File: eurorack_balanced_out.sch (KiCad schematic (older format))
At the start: 19 parts

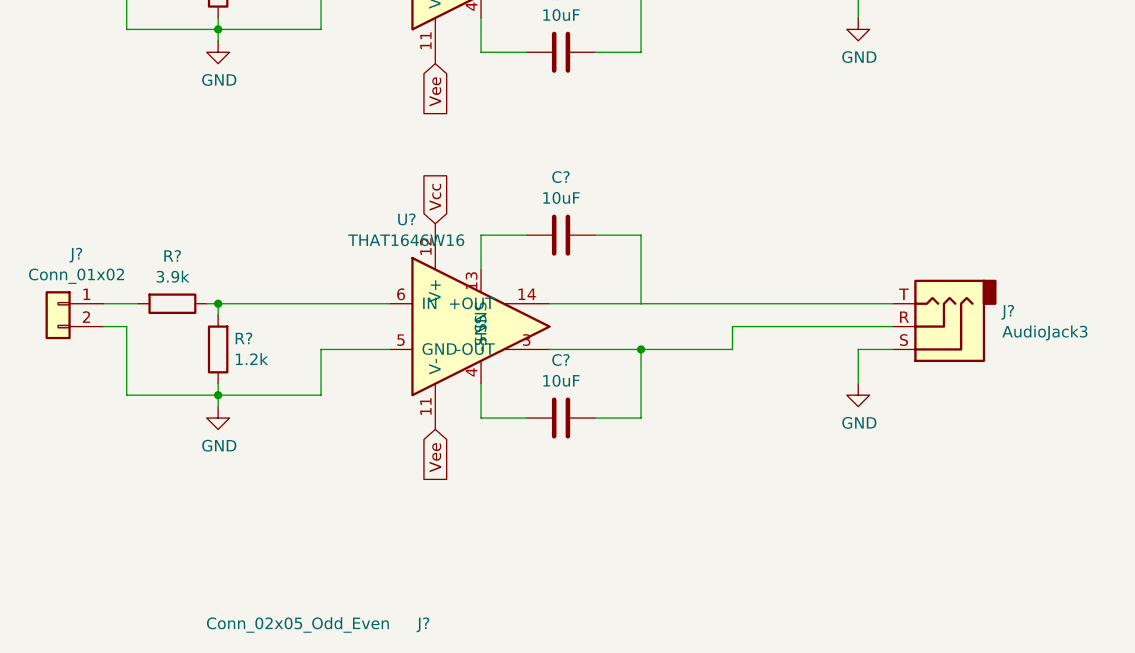
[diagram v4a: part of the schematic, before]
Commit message: delete a channel
we'll duplicate it again when we're done
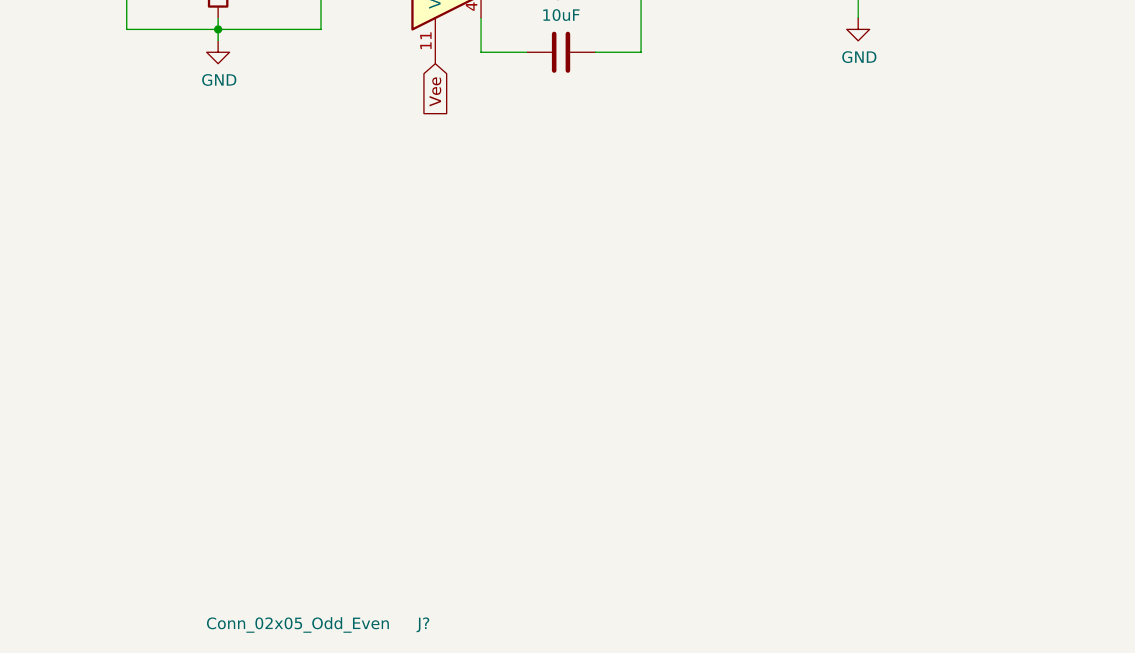
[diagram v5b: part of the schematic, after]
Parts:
- removed C? (x2): 10uF, Capacitor_SMD:CP_Elec_5x5.4, symbol Device:C
- removed J?: Conn_01x02, symbol Connector_Generic:Conn_01x02
- removed J?: AudioJack3, Connector_Audio:Jack_6.35mm_Neutrik_NJ3FD-V_Vertical, symbol Connector:AudioJack3
- removed R?: 1.2k, Resistor_SMD:R_0805_2012Metric_Pad1.15x1.40mm_HandSolder, symbol Device:R
- removed R?: 3.9k, Resistor_SMD:R_0805_2012Metric_Pad1.15x1.40mm_HandSolder, symbol Device:R
- removed U?: THAT1646W16, Package_SO:SOIC-16W_7.5x10.3mm_P1.27mm, symbol patchut:THAT1646W16
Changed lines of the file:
@@
 $EndComp
-$Comp
-L patchut:THAT1646W16 U?
-U 1 1 5EC6EB1D
-P 5000 3000
-F 0 "U?" H 4675 3467 50  0000 C CNN
-F 1 "THAT1646W16" H 4675 3376 50  0000 C CNN
-F 2 "Package_SO:SOIC-16W_7.5x10.3mm_P1.27mm" H 4850 3350 50  0001 C CNN
-F 3 "http://www.thatcorp.com/datashts/THAT_1606-1646_Datasheet.pdf" H 4850 3350 50  0001 C CNN
-	1    5000 3000
-	1    0    0    -1
-$EndComp
-$Comp
-L Device:C C?
-U 1 1 5EC6EB24
-P 5350 2600
-F 0 "C?" V 5098 2600 50  0000 C CNN
-F 1 "10uF" V 5189 2600 50  0000 C CNN
-F 2 "Capacitor_SMD:CP_Elec_5x5.4" H 5388 2450 50  0001 C CNN
-F 3 "~" H 5350 2600 50  0001 C CNN
-F 4 "647-UWP1C100MCL" V 5350 2600 50  0001 C CNN "Mouser"
-	1    5350 2600
-	0    1    1    0
-$EndComp
-Wire Wire Line
-	5200 2600 5000 2600
-Wire Wire Line
-	5000 2600 5000 2750
-Wire Wire Line
-	5300 2900 5700 2900
-Wire Wire Line
-	5700 2900 5700 2600
-Wire Wire Line
-	5700 2600 5500 2600
-$Comp
-L Device:C C?
-U 1 1 5EC6EB30
-P 5350 3400
-F 0 "C?" V 5098 3400 50  0000 C CNN
-F 1 "10uF" V 5189 3400 50  0000 C CNN
-F 2 "Capacitor_SMD:CP_Elec_5x5.4" H 5388 3250 50  0001 C CNN
-F 3 "~" H 5350 3400 50  0001 C CNN
-F 4 "647-UWP1C100MCL" V 5350 3400 50  0001 C CNN "Mouser"
-	1    5350 3400
-	0    1    1    0
-$EndComp
-Wire Wire Line
-	5000 3250 5000 3400
-Wire Wire Line
-	5000 3400 5200 3400
-Wire Wire Line
-	5500 3400 5700 3400
-Wire Wire Line
-	5700 3400 5700 3100
-Wire Wire Line
-	5700 3100 5300 3100
-Text GLabel 4800 3450 3    50   Input ~ 0
-Vee
-Text GLabel 4800 2550 1    50   Input ~ 0
-Vcc
 $Comp
 L Connector_Generic:Conn_02x05_Odd_Even J?
@@
 	3850 1700 4300 1700
 $Comp
-L power:GND #PWR?
-U 1 1 5ECB48AD
-P 3850 3350
-F 0 "#PWR?" H 3850 3100 50  0001 C CNN
-F 1 "GND" H 3855 3177 50  0000 C CNN
-F 2 "" H 3850 3350 50  0001 C CNN
-F 3 "" H 3850 3350 50  0001 C CNN
-	1    3850 3350
-	1    0    0    -1
-$EndComp
-$Comp
-L Connector_Generic:Conn_01x02 J?
-U 1 1 5ECB48B3
-P 3150 2900
-F 0 "J?" H 3068 3117 50  0000 C CNN
-F 1 "Conn_01x02" H 3068 3026 50  0000 C CNN
-F 2 "" H 3150 2900 50  0001 C CNN
-F 3 "~" H 3150 2900 50  0001 C CNN
-	1    3150 2900
-	-1   0    0    -1
-$EndComp
-Wire Wire Line
-	3500 2900 3350 2900
-Wire Wire Line
-	3800 2900 3850 2900
-Wire Wire Line
-	3850 2950 3850 2900
-Connection ~ 3850 2900
-Wire Wire Line
-	3850 2900 4600 2900
-Wire Wire Line
-	3850 3250 3850 3300
-Connection ~ 3850 3300
-Wire Wire Line
-	3850 3300 3850 3350
-Wire Wire Line
-	3350 3000 3450 3000
-Wire Wire Line
-	3450 3000 3450 3300
-Wire Wire Line
-	3450 3300 3850 3300
-Wire Wire Line
-	3850 3300 4300 3300
-Wire Wire Line
-	4300 3300 4300 3100
-Wire Wire Line
-	4300 3100 4600 3100
-$Comp
 L Device:R R?
 U 1 1 5ECB87DC
@@
 	-1   0    0    1
 $EndComp
-$Comp
-L Device:R R?
-U 1 1 5ECB902C
-P 3850 3100
-F 0 "R?" H 3780 3054 50  0000 R CNN
-F 1 "1.2k" H 3780 3145 50  0000 R CNN
-F 2 "Resistor_SMD:R_0805_2012Metric_Pad1.15x1.40mm_HandSolder" V 3780 3100 50  0001 C CNN
-F 3 "~" H 3850 3100 50  0001 C CNN
-	1    3850 3100
-	-1   0    0    1
-$EndComp
-$Comp
-L Device:R R?
-U 1 1 5ECB9314
-P 3650 2900
-F 0 "R?" V 3443 2900 50  0000 C CNN
-F 1 "3.9k" V 3534 2900 50  0000 C CNN
-F 2 "Resistor_SMD:R_0805_2012Metric_Pad1.15x1.40mm_HandSolder" V 3580 2900 50  0001 C CNN
-F 3 "~" H 3650 2900 50  0001 C CNN
-	1    3650 2900
-	0    1    1    0
-$EndComp
 Wire Wire Line
 	6800 1300 5700 1300
@@
 $Comp
 L Connector:AudioJack3 J?
-U 1 1 5ECCD754
-P 7000 3000
-F 0 "J?" H 6720 2933 50  0000 R CNN
-F 1 "AudioJack3" H 6720 3024 50  0000 R CNN
-F 2 "Connector_Audio:Jack_6.35mm_Neutrik_NJ3FD-V_Vertical" H 7000 3000 50  0001 C CNN
-F 3 "~" H 7000 3000 50  0001 C CNN
-	1    7000 3000
-	-1   0    0    1
-$EndComp
-Wire Wire Line
-	6800 2900 5700 2900
-Wire Wire Line
-	6800 3000 6100 3000
-$Comp
-L power:GND #PWR?
-U 1 1 5ECCD75C
-P 6650 3250
-F 0 "#PWR?" H 6650 3000 50  0001 C CNN
-F 1 "GND" H 6655 3077 50  0000 C CNN
-F 2 "" H 6650 3250 50  0001 C CNN
-F 3 "" H 6650 3250 50  0001 C CNN
-	1    6650 3250
-	1    0    0    -1
-$EndComp
-Wire Wire Line
-	6800 3100 6650 3100
-Wire Wire Line
-	6650 3100 6650 3250
-Wire Wire Line
-	5700 3100 6100 3100
-Wire Wire Line
-	6100 3100 6100 3000
-Connection ~ 5700 3100
-$Comp
-L Connector:AudioJack3 J?

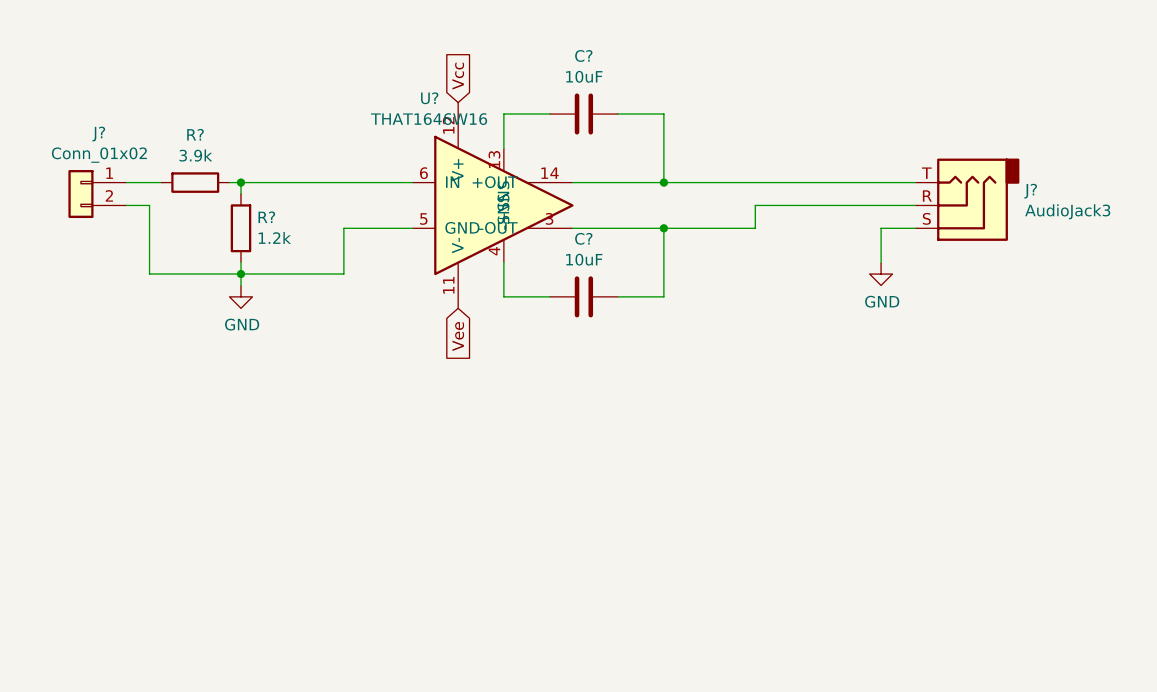
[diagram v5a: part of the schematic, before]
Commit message: add output protection diodes
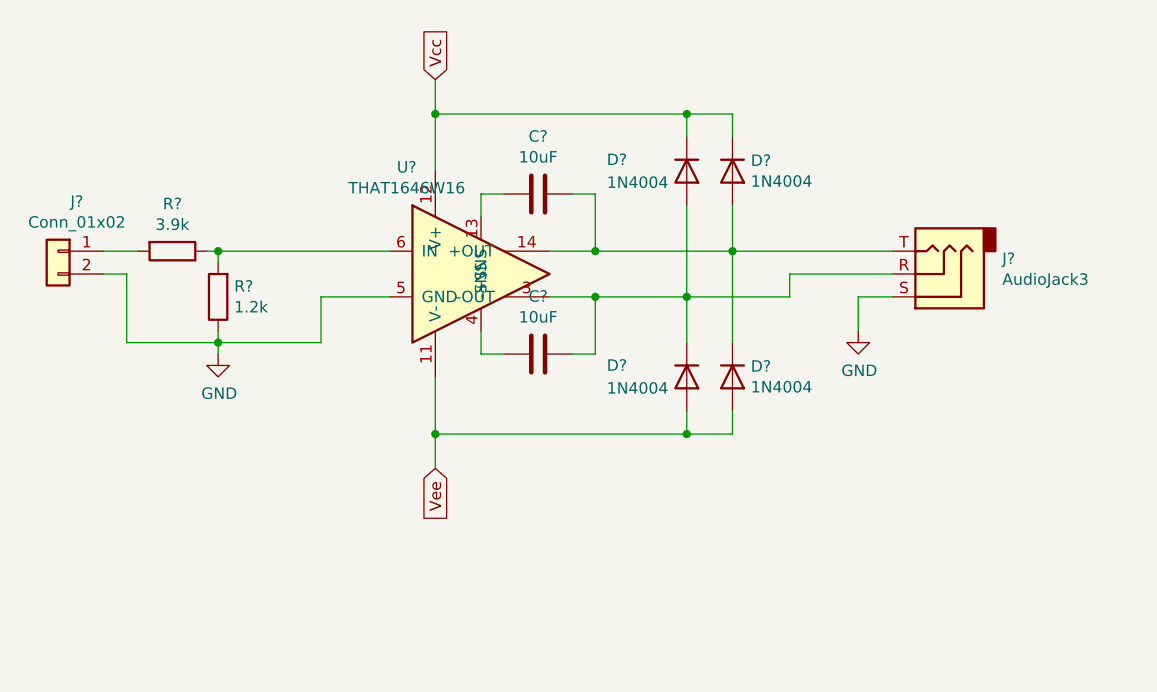
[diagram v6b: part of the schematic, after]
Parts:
- added D? (x4): 1N4004, Diode_THT:D_DO-41_SOD81_P10.16mm_Horizontal, symbol Diode:1N4004
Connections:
- net Vcc: now also D?.1 (K), D?.1 (K)
- net Vee: now also D?.2 (A), D?.2 (A)
- net at C?.1, J?.T, U?.14 (+OUT): now also D?.1 (K), D?.2 (A)
- net at C?.1, J?.R, U?.3 (-OUT): now also D?.1 (K), D?.2 (A)
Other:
- moved on the sheet: C?, J?, R?, U?

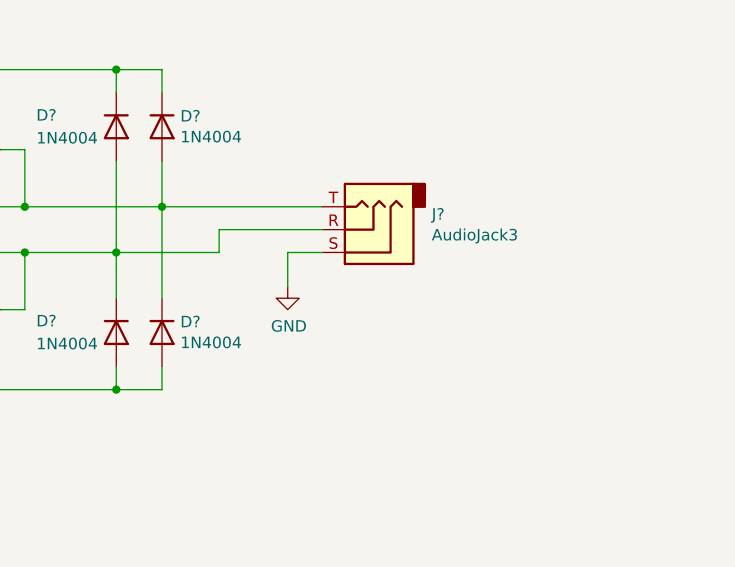
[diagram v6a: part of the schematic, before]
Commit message: output emc filtering
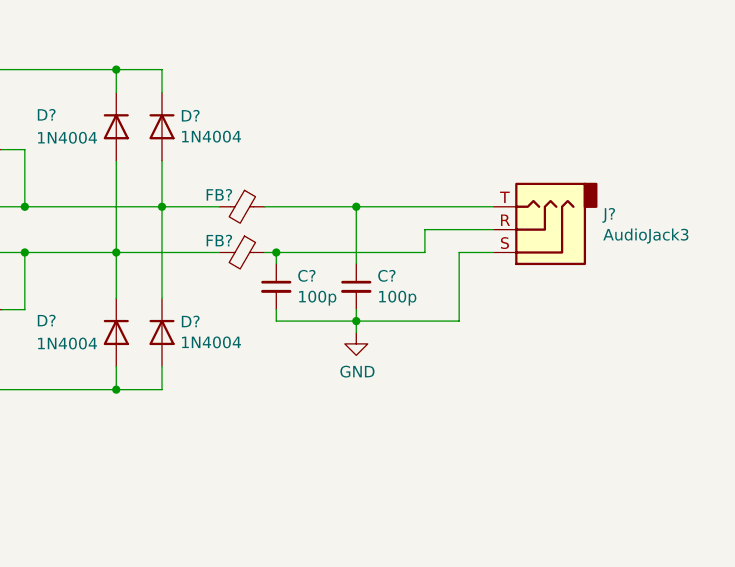
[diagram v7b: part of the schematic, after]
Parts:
- added C? (x2): 100p, Capacitor_SMD:C_0805_2012Metric_Pad1.15x1.40mm_HandSolder, symbol Device:C_Small
- added FB? (x2): 600R @ 100Mhz, Resistor_SMD:R_0805_2012Metric_Pad1.15x1.40mm_HandSolder, symbol Device:Ferrite_Bead_Small
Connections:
- net GND: now also C?.2, C?.2
- net at C?.1, D?.1 (K), D?.2 (A)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: now also FB?.2; no longer J?.T
- net at C?.1, D?.1 (K), D?.2 (A)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: now also FB?.2; no longer J?.R
- new net: C?.1, FB?.1, J?.R
- new net: C?.1, FB?.1, J?.T
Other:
- moved on the sheet: J?
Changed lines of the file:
@@
 L power:GND #PWR?
 U 1 1 5ECC7C45
-P 6550 1950
-F 0 "#PWR?" H 6550 1700 50  0001 C CNN
-F 1 "GND" H 6555 1777 50  0000 C CNN
-F 2 "" H 6550 1950 50  0001 C CNN
-F 3 "" H 6550 1950 50  0001 C CNN
-	1    6550 1950
+P 6850 2150
+F 0 "#PWR?" H 6850 1900 50  0001 C CNN
+F 1 "GND" H 6855 1977 50  0000 C CNN
+F 2 "" H 6850 2150 50  0001 C CNN
+F 3 "" H 6850 2150 50  0001 C CNN
+	1    6850 2150
 	1    0    0    -1
 $EndComp
 Wire Wire Line
-	6700 1800 6550 1800
-Wire Wire Line
-	6550 1800 6550 1950
+	7450 1800 7300 1800
 $Comp
 L Connector:AudioJack3 J?
 U 1 1 5EC84302
-P 6900 1700
-F 0 "J?" H 6620 1633 50  0000 R CNN
-F 1 "AudioJack3" H 6620 1724 50  0000 R CNN
-F 2 "Connector_Audio:Jack_6.35mm_Neutrik_NJ3FD-V_Vertical" H 6900 1700 50  0001 C CNN
-F 3 "~" H 6900 1700 50  0001 C CNN
-	1    6900 1700
+P 7650 1700
+F 0 "J?" H 7370 1633 50  0000 R CNN
+F 1 "AudioJack3" H 7370 1724 50  0000 R CNN
+F 2 "Connector_Audio:Jack_6.35mm_Neutrik_NJ3FD-V_Vertical" H 7650 1700 50  0001 C CNN
+F 3 "~" H 7650 1700 50  0001 C CNN
+	1    7650 1700
 	-1   0    0    1
 $EndComp
@@
 	0    1    1    0
 $EndComp
+Wire Wire Line
+	5400 1800 5800 1800
+Wire Wire Line
+	5800 1000 5800 1100
+Wire Wire Line
+	5800 1000 6000 1000
+Wire Wire Line
+	6000 1000 6000 1100
+Wire Wire Line
+	5800 2300 5800 2400
+Wire Wire Line
+	5800 2400 6000 2400
+Wire Wire Line
+	6000 2400 6000 2300
+Wire Wire Line
+	5800 1000 4700 1000
+Wire Wire Line
+	4700 1000 4700 1250
+Connection ~ 5800 1000
+Wire Wire Line
+	5800 2400 4700 2400
+Wire Wire Line
+	4700 2400 4700 2150
+Connection ~ 5800 2400
+Wire Wire Line
+	5800 2000 5800 1800
+Connection ~ 5800 1800
+Wire Wire Line
+	5800 1800 6250 1800
+Wire Wire Line
+	5800 1800 5800 1400
+Wire Wire Line
+	6000 1400 6000 1600
+Connection ~ 6000 1600
+Wire Wire Line
+	6000 1600 6000 2000
+Wire Wire Line
+	4700 850  4700 1000
+Connection ~ 4700 1000
+Wire Wire Line
+	4700 2550 4700 2400
+Connection ~ 4700 2400
+$Comp
+L Device:Ferrite_Bead_Small FB?
+U 1 1 5EC871B4
+P 6350 1600
+F 0 "FB?" V 6300 1500 50  0000 C CNN
+F 1 "600R @ 100Mhz" V 6450 1650 50  0001 C CNN
+F 2 "Resistor_SMD:R_0805_2012Metric_Pad1.15x1.40mm_HandSolder" V 6280 1600 50  0001 C CNN
+F 3 "~" H 6350 1600 50  0001 C CNN
+F 4 " 81-BLM21A601F" V 6350 1600 50  0001 C CNN "Mouser"
+	1    6350 1600
+	0    1    1    0
+$EndComp
+Wire Wire Line
+	6250 1600 6000 1600
+$Comp
+L Device:C_Small C?
+U 1 1 5EC892F5
+P 6500 1950
+F 0 "C?" H 6592 1996 50  0000 L CNN
+F 1 "100p" H 6592 1905 50  0000 L CNN
+F 2 "Capacitor_SMD:C_0805_2012Metric_Pad1.15x1.40mm_HandSolder" H 6500 1950 50  0001 C CNN
+F 3 "~" H 6500 1950 50  0001 C CNN
+F 4 " 80-C0805C101JAGAUTO " H 6500 1950 50  0001 C CNN "Mouser"
+	1    6500 1950
+	1    0    0    -1
+$EndComp
+Wire Wire Line
+	7150 1800 7150 1700
+Wire Wire Line
+	7150 1700 7450 1700
+Wire Wire Line
+	6450 1600 6850 1600
+Wire Wire Line
+	6450 1800 6500 1800
+Wire Wire Line
+	6850 2150 6850 2100
+Wire Wire Line
+	6850 2100 7300 2100
+Wire Wire Line
+	7300 1800 7300 2100
+Connection ~ 6850 2100
+Wire Wire Line
+	6850 2100 6850 2050
+Wire Wire Line
+	6850 2100 6500 2100
+Wire Wire Line
+	6500 2100 6500 2050
+Wire Wire Line
+	6500 1850 6500 1800
+Connection ~ 6500 1800
+Wire Wire Line
+	6500 1800 7150 1800
+Wire Wire Line
+	6850 1850 6850 1600
+Connection ~ 6850 1600
+Wire Wire Line
+	6850 1600 7450 1600
 $Comp
 L Diode:1N4004 D?
@@
 	0    1    1    0
 $EndComp
-Wire Wire Line
-	6250 1800 6250 1700
-Wire Wire Line
-	6250 1700 6700 1700
-Wire Wire Line
-	5400 1800 5800 1800
-Wire Wire Line
-	5800 1000 5800 1100
-Wire Wire Line
-	5800 1000 6000 1000
-Wire Wire Line
-	6000 1000 6000 1100
-Wire Wire Line
-	5800 2300 5800 2400
-Wire Wire Line
-	5800 2400 6000 2400
-Wire Wire Line
-	6000 2400 6000 2300
-Wire Wire Line
-	5800 1000 4700 1000
-Wire Wire Line
-	4700 1000 4700 1250
-Connection ~ 5800 1000
-Wire Wire Line
-	5800 2400 4700 2400
-Wire Wire Line
-	4700 2400 4700 2150
-Connection ~ 5800 2400
-Wire Wire Line
-	5800 2000 5800 1800
-Connection ~ 5800 1800
-Wire Wire Line
-	5800 1800 6250 1800
-Wire Wire Line
-	5800 1800 5800 1400
-Wire Wire Line
-	6000 1400 6000 1600
-Connection ~ 6000 1600
-Wire Wire Line
-	6000 1600 6700 1600
-Wire Wire Line
-	6000 1600 6000 2000
-Wire Wire Line
-	4700 850  4700 1000
-Connection ~ 4700 1000
-Wire Wire Line
-	4700 2550 4700 2400
-Connection ~ 4700 2400
+$Comp
+L Device:Ferrite_Bead_Small FB?
+U 1 1 5ECA915E
+P 6350 1800
+F 0 "FB?" V 6300 1700 50  0000 C CNN
+F 1 "600R @ 100Mhz" V 6450 1850 50  0001 C CNN
+F 2 "Resistor_SMD:R_0805_2012Metric_Pad1.15x1.40mm_HandSolder" V 6280 1800 50  0001 C CNN
+F 3 "~" H 6350 1800 50  0001 C CNN
+F 4 " 81-BLM21A601F" V 6350 1800 50  0001 C CNN "Mouser"
+	1    6350 1800
+	0    1    1    0
+$EndComp
+$Comp
+L Device:C_Small C?
+U 1 1 5ECA9863
+P 6850 1950
+F 0 "C?" H 6942 1996 50  0000 L CNN
+F 1 "100p" H 6942 1905 50  0000 L CNN
+F 2 "Capacitor_SMD:C_0805_2012Metric_Pad1.15x1.40mm_HandSolder" H 6850 1950 50  0001 C CNN
+F 3 "~" H 6850 1950 50  0001 C CNN
+F 4 " 80-C0805C101JAGAUTO " H 6850 1950 50  0001 C CNN "Mouser"
+	1    6850 1950
+	1    0    0    -1
+$EndComp
 $EndSCHEMATC
